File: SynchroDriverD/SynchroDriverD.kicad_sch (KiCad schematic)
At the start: 35 parts, among them J1 SYNC, J2 POWER, J3 ROLL, J4 PITCH, J5 YAW, J6 NEEDLES, J7 FLAG, U1 Teensy4_1, U10 173010542, U2 LM324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

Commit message: Ad flag drive circuit
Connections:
- net FlagDriver/OUT: now reaches J7.2 (Pin_2)
- net FLAG: now reaches U1.18 (GP26)
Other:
- sheet FlagDriver ports: added IN, OUT; removed none
- moved on the sheet: J7, R1, R2, U2A

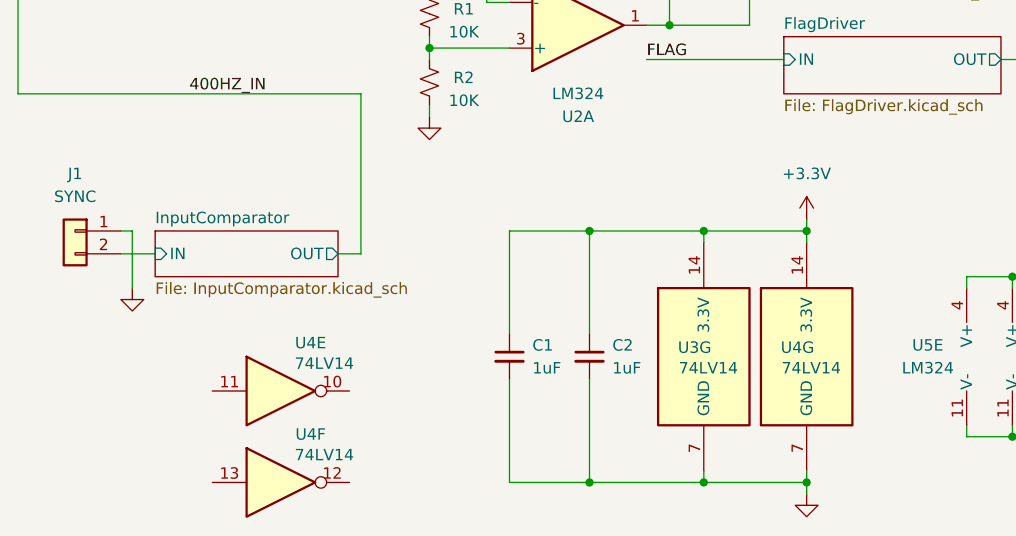
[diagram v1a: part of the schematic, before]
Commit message: Swap DRV8300 for DRV8300DI, change ref in
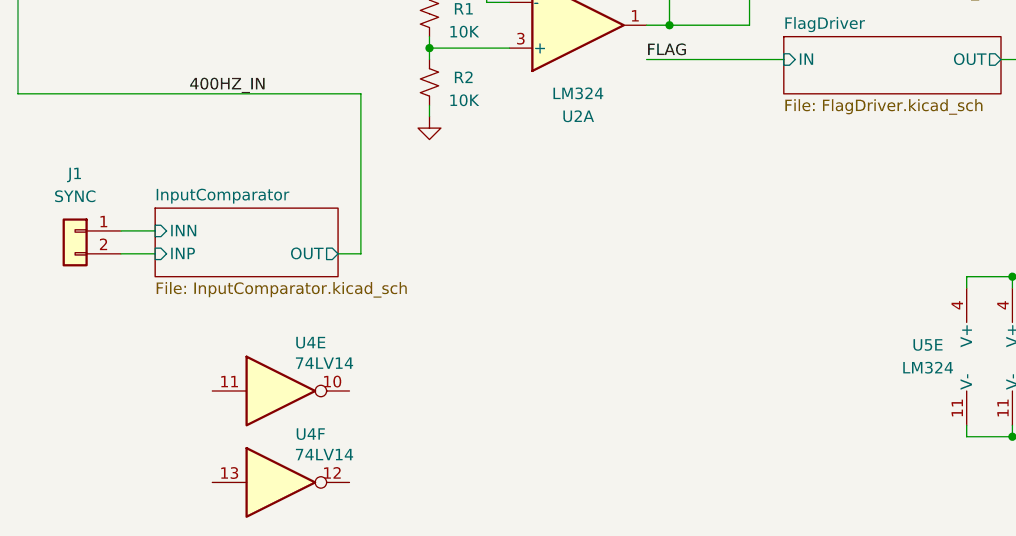
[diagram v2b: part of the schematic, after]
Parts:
- removed C1, C2: 1uF, Passive:CAPC2012X55, symbol Device:C_Small
- removed U3: 74LV14, Active:SOP127P620X175-14, symbol 74xx:74LV14
- removed unit 7 of U4
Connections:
- net GND: no longer J1.1 (Pin_1)
- net InputComparator/IN renamed InputComparator/INP
- new net InputComparator/INN: J1.1 (Pin_1)
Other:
- sheet InputComparator ports: added INN, INP; removed IN

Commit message: Improve ref in, clearance for 115V
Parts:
- removed U4: 74LV14, Active:SOP127P620X175-14, symbol 74xx:74LV14
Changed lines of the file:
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@@
-	)
-	(symbol
-		(lib_id "74xx:74LV14")
-		(at 48.26 189.23 0)
-		(unit 6)
-		(exclude_from_sim no)
-		(in_bom yes)
-		(on_board yes)
-		(dnp no)
-		(property "Reference" "U4"
-			(at 51.562 183.896 0)
-			(effects
-				(font
-					(size 1.27 1.27)
-				)
-			)
-		)
-		(property "Value" "74LV14"
-			(at 53.086 186.182 0)
-			(effects
-				(font
-					(size 1.27 1.27)
-				)
-			)
-		)
-		(property "Footprint" "Active:SOP127P620X175-14"
-			(at 48.26 189.23 0)
-			(effects
-				(font
-					(size 1.27 1.27)
-				)
-				(hide yes)
-			)
-		)
-		(property "Datasheet" "http://www.ti.com/lit/gpn/sn74LV14"
-			(at 48.26 189.23 0)
-			(effects
-				(font
-					(size 1.27 1.27)
-				)
-				(hide yes)
-			)
-		)
-		(property "Description" "Hex Inverter"
-			(at 48.26 189.23 0)
-			(effects
-				(font
-					(size 1.27 1.27)
-				)
-				(hide yes)
-			)
-		)
-		(pin "7"
-		)
-		(pin "2"
-		)
-		(pin "5"
-		)
-		(pin "8"
-		)
-		(pin "3"
-		)
-		(pin "10"
-		)
-		(pin "9"
-		)
-		(pin "6"
-		)
-		(pin "13"
-		)
-		(pin "14"
-		)
-		(pin "4"
-		)
-		(pin "11"
-		)
-		(pin "1"
-		)
-		(pin "12"
-		)
-		(instances
-			(project "SynchroDriverD"
-				(path "/cf120ebf-5c4f-4079-9e7c-fed8dabc289c"
-					(reference "U4")
-					(unit 6)
-				)
-			)
-		)
 	)
 	(symbol
@@
 				)
 			)
-		)
-	)
-	(symbol
-		(lib_id "74xx:74LV14")
-		(at 48.26 179.07 0)
-		(unit 5)
-		(exclude_from_sim no)
-		(in_bom yes)
-		(on_board yes)
-		(dnp no)
-		(property "Reference" "U4"
-			(at 51.562 173.736 0)
-			(effects
-				(font
-					(size 1.27 1.27)
-				)
-			)
-		)
-		(property "Value" "74LV14"
-			(at 53.086 176.022 0)
-			(effects
-				(font
-					(size 1.27 1.27)
-				)
-			)
-		)
-		(property "Footprint" "Active:SOP127P620X175-14"
-			(at 48.26 179.07 0)
-			(effects
-				(font
-					(size 1.27 1.27)
-				)
-				(hide yes)
-			)
-		)
-		(property "Datasheet" "http://www.ti.com/lit/gpn/sn74LV14"
-			(at 48.26 179.07 0)
-			(effects
-				(font
-					(size 1.27 1.27)
-				)
-				(hide yes)
-			)
-		)
-		(property "Description" "Hex Inverter"
-			(at 48.26 179.07 0)
-			(effects
-				(font
-					(size 1.27 1.27)
-				)
-				(hide yes)
-			)
-		)
-		(pin "7"
-		)
-		(pin "2"
-		)
-		(pin "5"
-		)
-		(pin "8"
-		)
-		(pin "3"
-		)
-		(pin "10"
-		)
-		(pin "9"
-		)
-		(pin "6"
-		)
-		(pin "13"
-		)
-		(pin "14"
-		)
-		(pin "4"
-		)
-		(pin "11"
-		)
-		(pin "1"
-		)
-		(pin "12"
-		)
-		(instances
-			(project "SynchroDriverD"
-				(path "/cf120ebf-5c4f-4079-9e7c-fed8dabc289c"
-					(reference "U4")
-					(unit 5)
-				)
-			)

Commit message: Tweaks after first build
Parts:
- R2: value 10K -> 20K
- U2, U5: Mouser (none) -> 863-LM324DR2G
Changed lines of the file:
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@@
 			)
 		)
-		(property "Value" "10K"
+		(property "Value" "20K"
 			(at 68.58 146.812 0)
 			(effects
@@
 			)
 		)
+		(property "Mouser" "863-LM324DR2G"
+			(at 121.92 175.26 0)
+			(effects
+				(font
+					(size 1.27 1.27)
+				)
+				(hide yes)
+			)
+		)
 		(pin "1"
 		)
@@
 		)
 		(property "Description" "Low-Power, Quad-Operational Amplifiers, DIP-14/SOIC-14/SSOP-14"
+			(at 81.28 138.43 0)
+			(effects
+				(font
+					(size 1.27 1.27)
+				)
+				(hide yes)
+			)
+		)
+		(property "Mouser" "863-LM324DR2G"
 			(at 81.28 138.43 0)
 			(effects
@@
 			(at 127 175.26 0)
 			(effects
+				(font
+					(size 1.27 1.27)
+				)
+				(hide yes)
+			)
+		)
+		(property "Mouser" "863-LM324DR2G"
+			(at 127 175.26 0)
+			(effects

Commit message: Meter driver vref fix. Sync in gain fix.
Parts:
- R1: value 10K -> 20K
- R2: value 20K -> 10K
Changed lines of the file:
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@@
 			)
 		)
-		(property "Value" "20K"
+		(property "Value" "10K"
 			(at 68.58 146.812 0)
 			(effects
@@
 			)
 		)
-		(property "Value" "10K"
+		(property "Value" "20K"
 			(at 68.58 139.192 0)
 			(effects
